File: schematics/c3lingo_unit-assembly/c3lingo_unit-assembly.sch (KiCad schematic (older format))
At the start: 0 parts

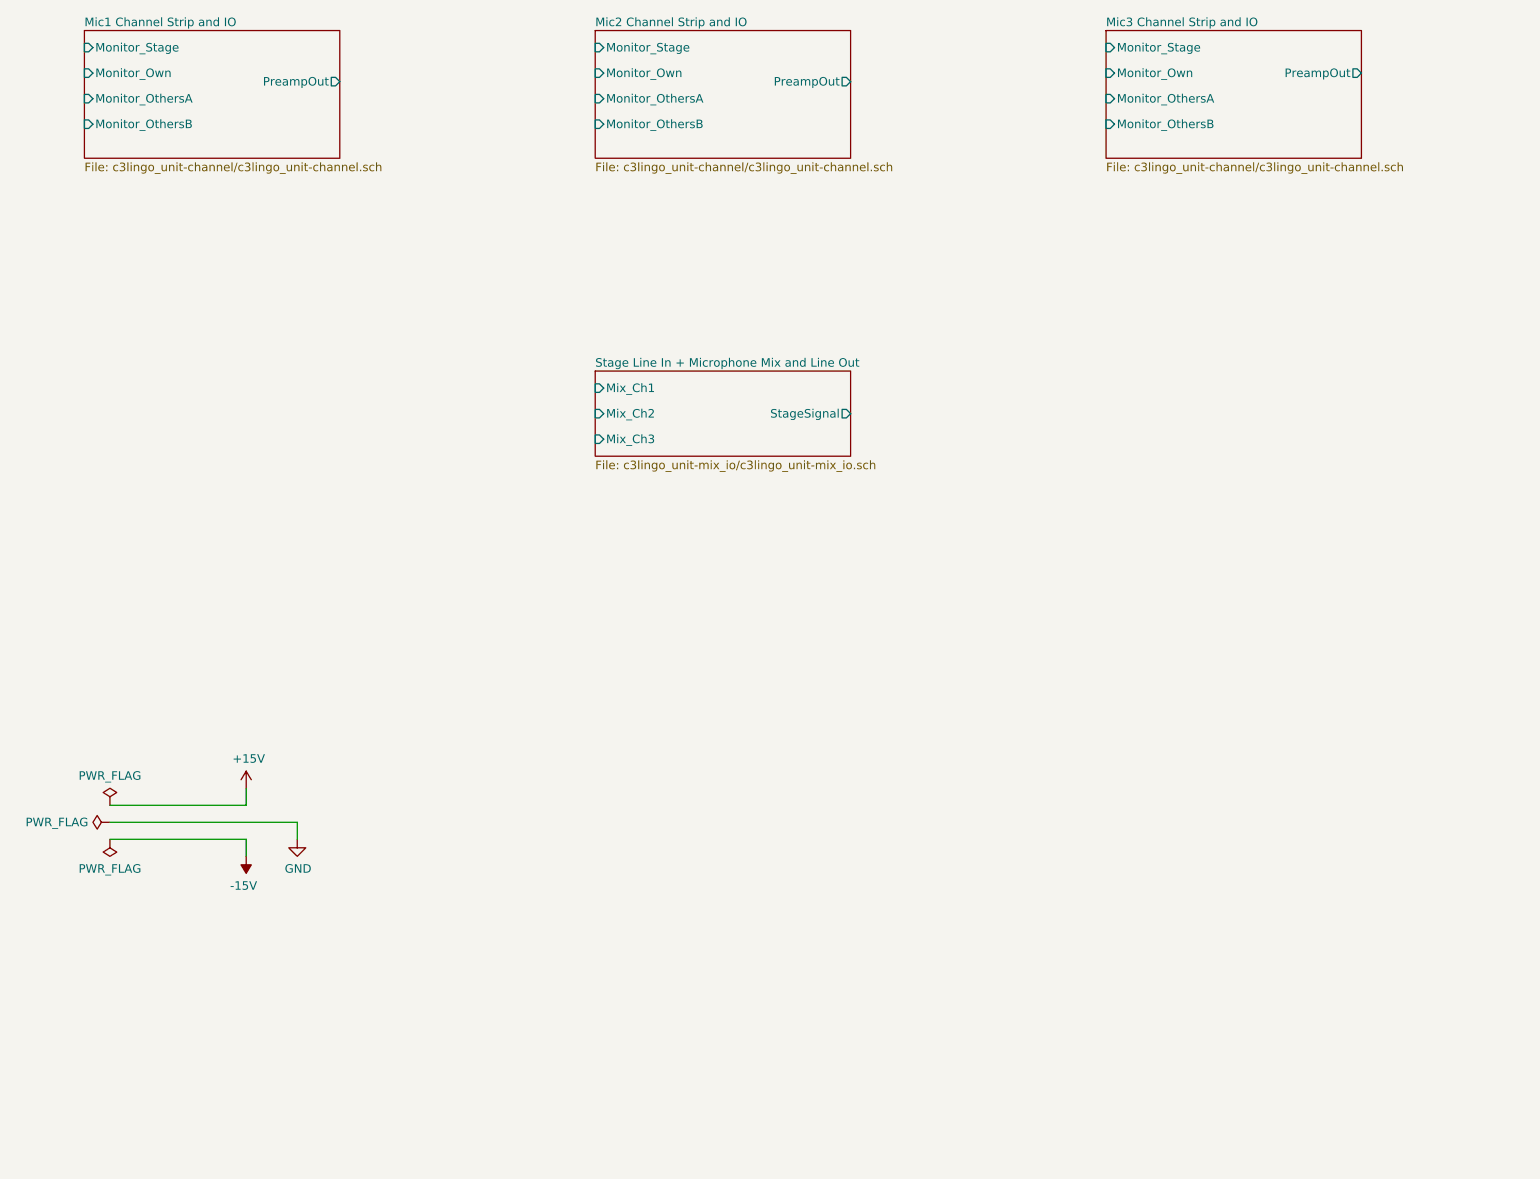
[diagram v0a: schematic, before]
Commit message: [TIDY] Channel Strip: Integrate VU Meter
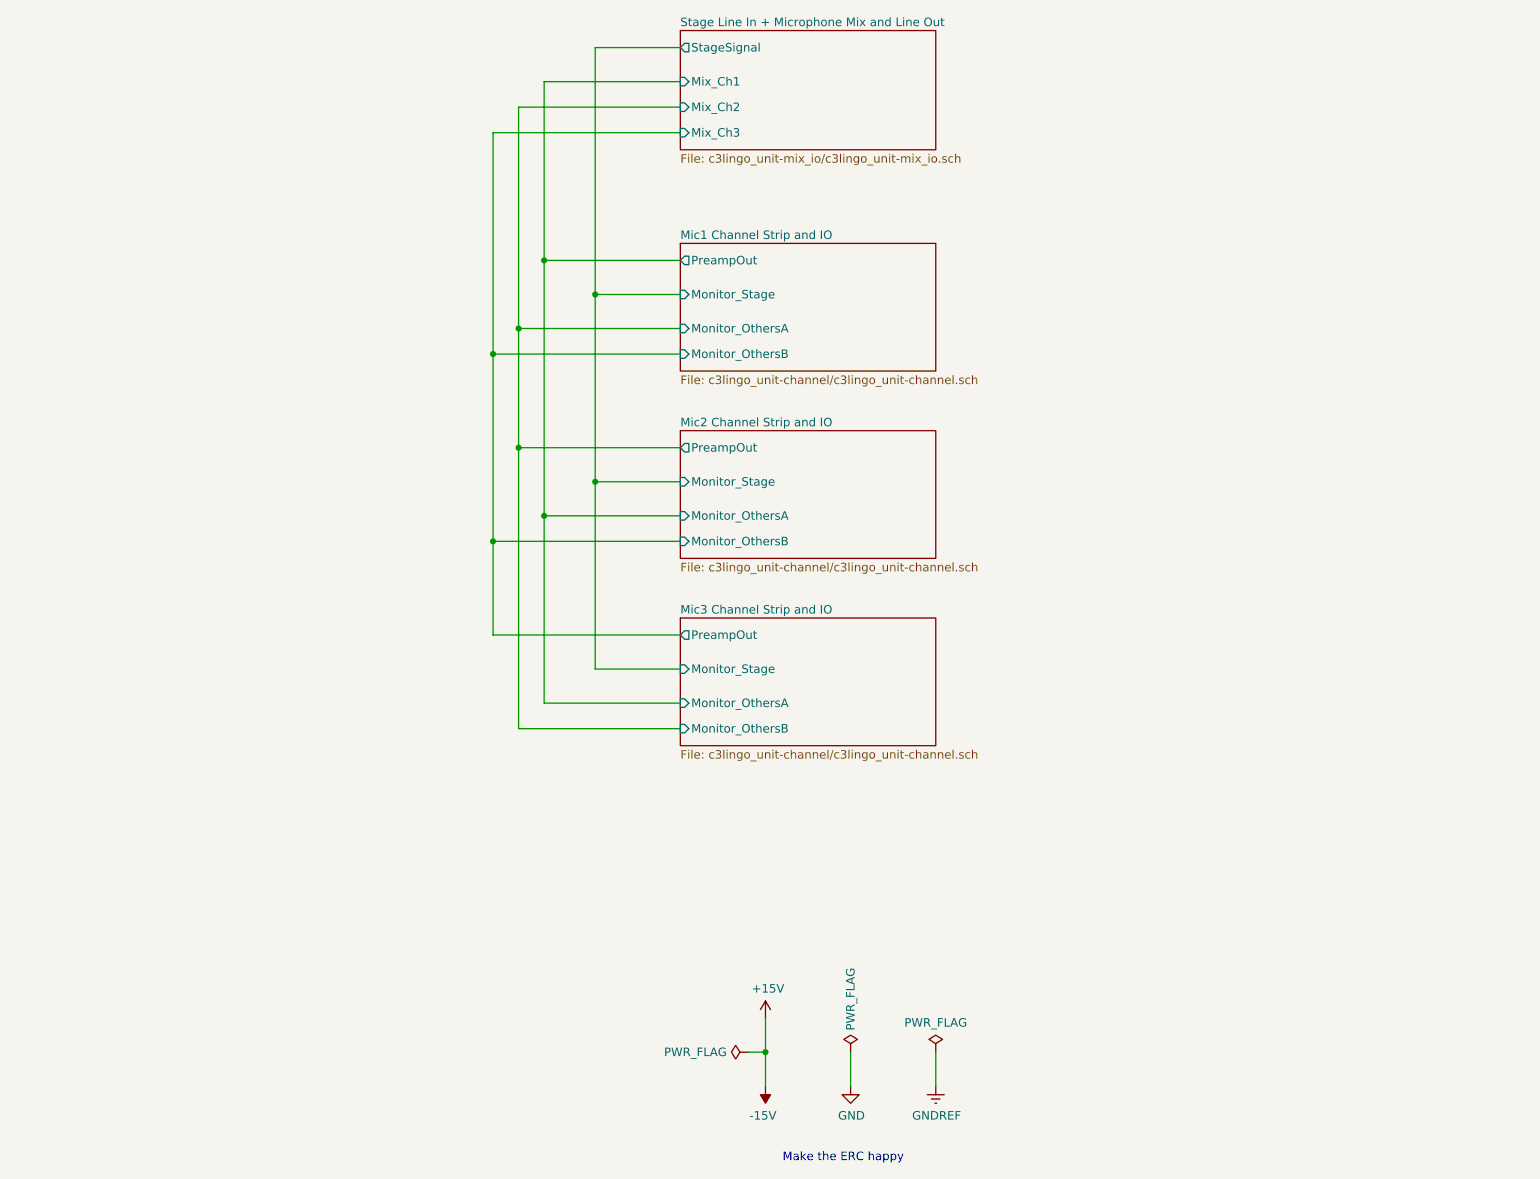
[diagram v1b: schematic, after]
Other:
- note added: "Make the ERC happy"
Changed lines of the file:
@@
 $EndDescr
 $Sheet
-S 4500 3000 1500 500
+S 5000 1000 1500 700
 U 60AE0DAE
 F0 "Stage Line In + Microphone Mix and Line Out" 50
 F1 "c3lingo_unit-mix_io/c3lingo_unit-mix_io.sch" 50
-F2 "StageSignal" O R 6000 3250 50
-F3 "Mix_Ch1" I L 4500 3100 50
-F4 "Mix_Ch2" I L 4500 3250 50
-F5 "Mix_Ch3" I L 4500 3400 50
-$EndSheet
-$Sheet
-S 1500 1000 1500 750
+F2 "StageSignal" O L 5000 1100 50
+F3 "Mix_Ch1" I L 5000 1300 50
+F4 "Mix_Ch2" I L 5000 1450 50
+F5 "Mix_Ch3" I L 5000 1600 50
+$EndSheet
+$Sheet
+S 5000 2250 1500 750
 U 60AA662F
 F0 "Mic1 Channel Strip and IO" 50
 F1 "c3lingo_unit-channel/c3lingo_unit-channel.sch" 50
-F2 "PreampOut" O R 3000 1300 50
-F3 "Monitor_Own" I L 1500 1250 50
-F4 "Monitor_OthersA" I L 1500 1400 50
-F5 "Monitor_OthersB" I L 1500 1550 50
-F6 "Monitor_Stage" I L 1500 1100 50
-$EndSheet
-$Sheet
-S 4500 1000 1500 750
+F2 "PreampOut" O L 5000 2350 50
+F3 "Monitor_OthersA" I L 5000 2750 50
+F4 "Monitor_OthersB" I L 5000 2900 50
+F5 "Monitor_Stage" I L 5000 2550 50
+$EndSheet
+$Sheet
+S 5000 3350 1500 750
 U 60AE7597
 F0 "Mic2 Channel Strip and IO" 50
 F1 "c3lingo_unit-channel/c3lingo_unit-channel.sch" 50
-F2 "PreampOut" O R 6000 1300 50
-F3 "Monitor_Own" I L 4500 1250 50
-F4 "Monitor_OthersA" I L 4500 1400 50
-F5 "Monitor_OthersB" I L 4500 1550 50
-F6 "Monitor_Stage" I L 4500 1100 50
-$EndSheet
-$Sheet
-S 7500 1000 1500 750
+F2 "PreampOut" O L 5000 3450 50
+F3 "Monitor_OthersA" I L 5000 3850 50
+F4 "Monitor_OthersB" I L 5000 4000 50
+F5 "Monitor_Stage" I L 5000 3650 50
+$EndSheet
+$Sheet
+S 5000 4450 1500 750
 U 60AE80F3
 F0 "Mic3 Channel Strip and IO" 50
 F1 "c3lingo_unit-channel/c3lingo_unit-channel.sch" 50
-F2 "PreampOut" O R 9000 1250 50
-F3 "Monitor_Own" I L 7500 1250 50
-F4 "Monitor_OthersA" I L 7500 1400 50
-F5 "Monitor_OthersB" I L 7500 1550 50
-F6 "Monitor_Stage" I L 7500 1100 50
+F2 "PreampOut" O L 5000 4550 50
+F3 "Monitor_OthersA" I L 5000 4950 50
+F4 "Monitor_OthersB" I L 5000 5100 50
+F5 "Monitor_Stage" I L 5000 4750 50
 $EndSheet
 $Comp
 L power:GND #PWR?
 U 1 1 60AC8130
-P 2750 5750
+P 6000 7200
 AR Path="/60AA662F/60AC8130" Ref="#PWR?"  Part="1"
 AR Path="/60AC8130" Ref="#PWR0101"  Part="1"
-F 0 "#PWR0101" H 2750 5500 50  0001 C CNN
-F 1 "GND" H 2755 5577 50  0000 C CNN
-F 2 "" H 2750 5750 50  0001 C CNN
-F 3 "" H 2750 5750 50  0001 C CNN
-	1    2750 5750
+F 0 "#PWR0101" H 6000 6950 50  0001 C CNN
+F 1 "GND" H 6005 7027 50  0000 C CNN
+F 2 "" H 6000 7200 50  0001 C CNN
+F 3 "" H 6000 7200 50  0001 C CNN
+	1    6000 7200
 	1    0    0    -1
 $EndComp
@@
 L power:+15V #PWR?
 U 1 1 60AC8136
-P 2450 5450
+P 5500 6800
 AR Path="/60AA662F/60AC8136" Ref="#PWR?"  Part="1"
 AR Path="/60AC8136" Ref="#PWR0102"  Part="1"
-F 0 "#PWR0102" H 2450 5300 50  0001 C CNN
-F 1 "+15V" H 2465 5623 50  0000 C CNN
-F 2 "" H 2450 5450 50  0001 C CNN
-F 3 "" H 2450 5450 50  0001 C CNN
-	1    2450 5450
+F 0 "#PWR0102" H 5500 6650 50  0001 C CNN
+F 1 "+15V" H 5515 6973 50  0000 C CNN
+F 2 "" H 5500 6800 50  0001 C CNN
+F 3 "" H 5500 6800 50  0001 C CNN
+	1    5500 6800
 	1    0    0    -1
 $EndComp
@@
 L power:-15V #PWR?
 U 1 1 60AC813C
-P 2450 5850
+P 5500 7200
 AR Path="/60AA662F/60AC813C" Ref="#PWR?"  Part="1"
 AR Path="/60AC813C" Ref="#PWR0103"  Part="1"
-F 0 "#PWR0103" H 2450 5950 50  0001 C CNN
-F 1 "-15V" H 2465 6023 50  0000 C CNN
-F 2 "" H 2450 5850 50  0001 C CNN
-F 3 "" H 2450 5850 50  0001 C CNN
-	1    2450 5850
+F 0 "#PWR0103" H 5500 7300 50  0001 C CNN
+F 1 "-15V" H 5515 7373 50  0000 C CNN
+F 2 "" H 5500 7200 50  0001 C CNN
+F 3 "" H 5500 7200 50  0001 C CNN
+	1    5500 7200
 	-1   0    0    1
 $EndComp
-Wire Wire Line
-	2450 5750 2450 5850
-Wire Wire Line
-	2450 5550 2450 5450
-Wire Wire Line
-	2750 5650 2750 5750
 $Comp
 L power:PWR_FLAG #FLG?
 U 1 1 60AC8148
-P 1650 5550
+P 5400 7000
 AR Path="/60AA662F/60AC8148" Ref="#FLG?"  Part="1"
 AR Path="/60AC8148" Ref="#FLG0104"  Part="1"
-F 0 "#FLG0104" H 1650 5625 50  0001 C CNN
-F 1 "PWR_FLAG" H 1650 5723 50  0000 C CNN
-F 2 "" H 1650 5550 50  0001 C CNN
-F 3 "~" H 1650 5550 50  0001 C CNN
-	1    1650 5550
-	1    0    0    -1
-$EndComp
+F 0 "#FLG0104" H 5400 7075 50  0001 C CNN
+F 1 "PWR_FLAG" V 5400 7127 50  0000 L CNN
+F 2 "" H 5400 7000 50  0001 C CNN
+F 3 "~" H 5400 7000 50  0001 C CNN
+	1    5400 7000
+	0    -1   -1   0
+$EndComp
+$Comp
+L power:PWR_FLAG #FLG?
+U 1 1 60AC8154
+P 6500 7000
+AR Path="/60AA662F/60AC8154" Ref="#FLG?"  Part="1"
+AR Path="/60AC8154" Ref="#FLG0106"  Part="1"
+F 0 "#FLG0106" H 6500 7075 50  0001 C CNN
+F 1 "PWR_FLAG" H 6500 7173 50  0000 C CNN
+F 2 "" H 6500 7000 50  0001 C CNN
+F 3 "~" H 6500 7000 50  0001 C CNN
+	1    6500 7000
+	1    0    0    -1
+$EndComp
+Text Notes 5600 7650 0    50   ~ 0
+Make the ERC happy
+$Comp
+L power:GNDREF #PWR090
+U 1 1 632B5377
+P 6500 7200
+F 0 "#PWR090" H 6500 6950 50  0001 C CNN
+F 1 "GNDREF" H 6505 7027 50  0000 C CNN
+F 2 "" H 6500 7200 50  0001 C CNN
+F 3 "" H 6500 7200 50  0001 C CNN
+	1    6500 7200
+	1    0    0    -1
+$EndComp
+Wire Wire Line
+	6500 7200 6500 7000
+Wire Wire Line
+	6000 7000 6000 7200
+Wire Wire Line
+	5500 6800 5500 7000
+Wire Wire Line
+	5500 7000 5400 7000
+Wire Wire Line
+	5500 7000 5500 7200
+Connection ~ 5500 7000
 $Comp
 L power:PWR_FLAG #FLG?
 U 1 1 60AC814E
-P 1650 5650
+P 6000 7000
 AR Path="/60AA662F/60AC814E" Ref="#FLG?"  Part="1"
 AR Path="/60AC814E" Ref="#FLG0105"  Part="1"
-F 0 "#FLG0105" H 1650 5725 50  0001 C CNN
-F 1 "PWR_FLAG" V 1650 5777 50  0000 L CNN
-F 2 "" H 1650 5650 50  0001 C CNN
-F 3 "~" H 1650 5650 50  0001 C CNN
-	1    1650 5650
-	0    -1   -1   0
-$EndComp
-$Comp
-L power:PWR_FLAG #FLG?
-U 1 1 60AC8154
-P 1650 5750
-AR Path="/60AA662F/60AC8154" Ref="#FLG?"  Part="1"
-AR Path="/60AC8154" Ref="#FLG0106"  Part="1"
-F 0 "#FLG0106" H 1650 5825 50  0001 C CNN
-F 1 "PWR_FLAG" H 1650 5923 50  0000 C CNN
-F 2 "" H 1650 5750 50  0001 C CNN
-F 3 "~" H 1650 5750 50  0001 C CNN
-	1    1650 5750
-	-1   0    0    1
-$EndComp
-Wire Wire Line
-	1650 5550 2450 5550
-Wire Wire Line
-	1650 5650 2750 5650
-Wire Wire Line
-	1650 5750 2450 5750
+F 0 "#FLG0105" H 6000 7075 50  0001 C CNN
+F 1 "PWR_FLAG" V 6000 7127 50  0000 L CNN
+F 2 "" H 6000 7000 50  0001 C CNN
+F 3 "~" H 6000 7000 50  0001 C CNN
+	1    6000 7000
+	1    0    0    -1
+$EndComp
+Wire Wire Line
+	5000 1100 4500 1100
+Wire Wire Line
+	4500 1100 4500 2550
+Wire Wire Line
+	4500 2550 5000 2550
+Wire Wire Line
+	4500 2550 4500 3650
+Wire Wire Line
+	4500 3650 5000 3650
+Connection ~ 4500 2550
+Wire Wire Line
+	4500 3650 4500 4750
+Wire Wire Line
+	4500 4750 5000 4750
+Connection ~ 4500 3650
+Wire Wire Line
+	5000 2350 4200 2350
+Wire Wire Line
+	4200 2350 4200 1300
+Wire Wire Line
+	4200 1300 5000 1300
+Wire Wire Line
+	5000 3450 4050 3450
+Wire Wire Line
+	4050 3450 4050 2750
+Wire Wire Line
+	4050 1450 5000 1450
+Wire Wire Line
+	5000 4550 3900 4550
+Wire Wire Line
+	3900 4550 3900 4000
+Wire Wire Line
+	3900 1600 5000 1600
+Wire Wire Line
+	4200 2350 4200 3850
+Wire Wire Line
+	4200 3850 5000 3850
+Connection ~ 4200 2350
+Wire Wire Line
+	4200 3850 4200 4950
+Wire Wire Line
+	4200 4950 5000 4950
+Connection ~ 4200 3850
+Wire Wire Line
+	4050 3450 4050 5100
+Wire Wire Line
+	4050 5100 5000 5100
+Connection ~ 4050 3450
+Wire Wire Line
+	4050 2750 5000 2750
+Connection ~ 4050 2750
+Wire Wire Line
+	4050 2750 4050 1450
+Wire Wire Line
+	3900 2900 5000 2900
+Connection ~ 3900 2900
+Wire Wire Line
+	3900 2900 3900 1600
+Wire Wire Line
+	5000 4000 3900 4000
+Connection ~ 3900 4000
+Wire Wire Line
+	3900 4000 3900 2900
 $EndSCHEMATC
